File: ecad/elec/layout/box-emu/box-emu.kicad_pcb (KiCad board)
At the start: 2 copper layers, 72.5 x 63.9 mm, 68 parts

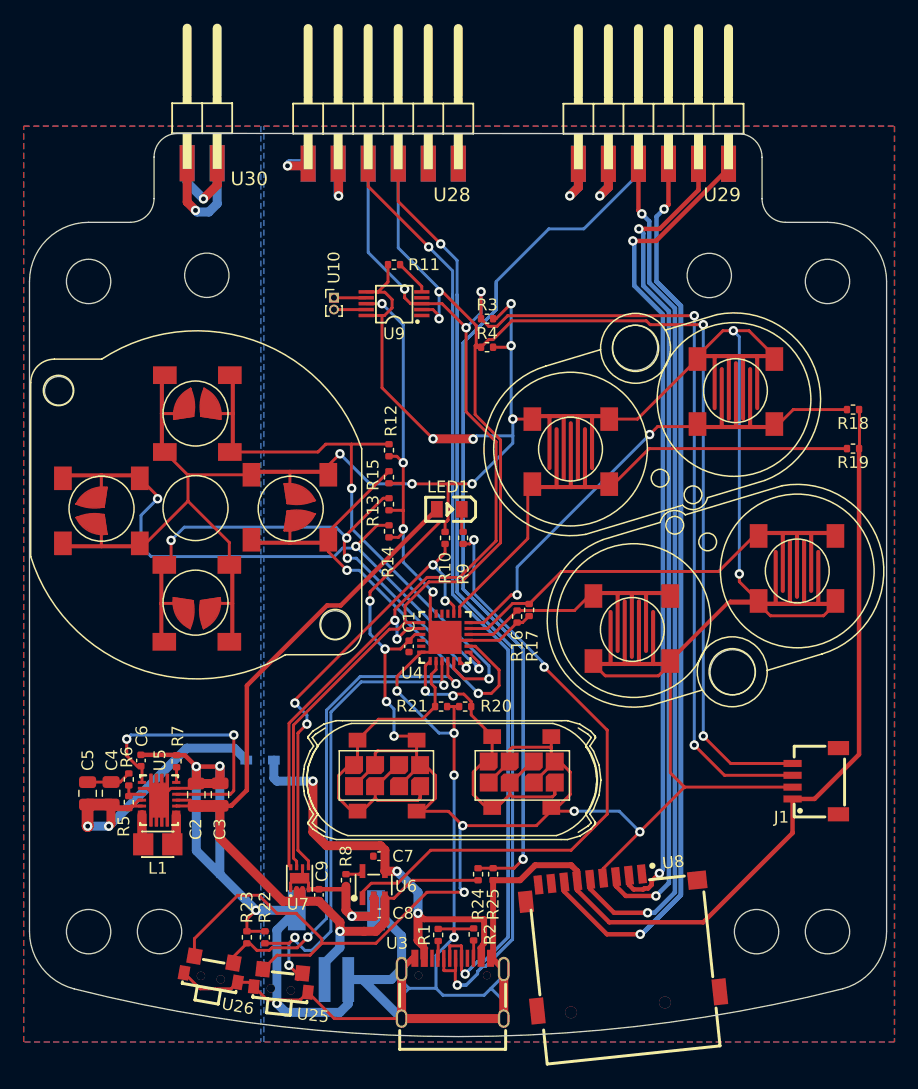
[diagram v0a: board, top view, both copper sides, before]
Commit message: Fix/atopile ecad (#82)
* fix(ecad): Fix bugs in atopile version of the design
* Add missing pullup resistors to AW9523 RSTN and INTN lines
* Fix I/O configuration for AW9523 so that all the inputs go to the same port pins as the previous version of the electronics

* minor cleanup to box3 after update to at 0.2.58

* fix udpate max17038 pullup to properly go to alert line after other fix

* typo

* update layout

* minor update to layout

* fix(buttons): pulldown -> pullup (so they are active low)

* update buttons to be pullup instead of pulldown; change led to be powered off VBUS instead of vbat

* update button footprints - start/select better aligned and all buttons have extra wires to ensure connections

* add net names and ensure packages are specified

* update box-emu-base layout

* update box-emu and box-3-emu layouts

* udpate to kicad 8

* add net name overrides and update all boards

* update atopile action to kicad 8

* comment out blender render
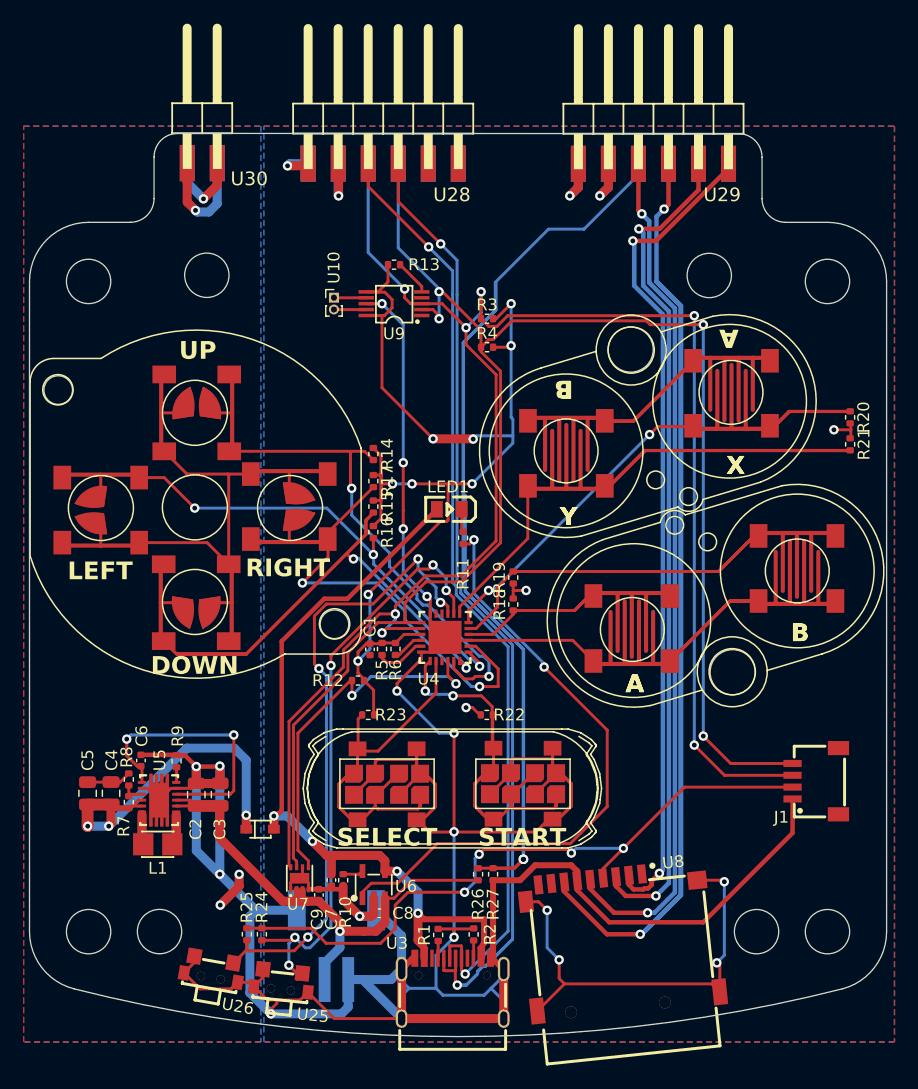
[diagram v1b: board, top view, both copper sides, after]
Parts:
- removed the R12 at (140.4, 96.7)
- removed the R13 at (140.4, 101.3)
- added R24: 62.5mW Thick Film Resistors 50V ±100ppm/℃ ±1% 10kΩ 0402 Chi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, lib:R0402, F.Cu at (129.7, 137.6)
- added R25: 62.5mW Thick Film Resistors 50V ±100ppm/℃ ±1% 10kΩ 0402 Chi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, lib:R0402, F.Cu at (128.4, 137.6)
- added R5: 62.5mW Thick Film Resistors 50V ±100ppm/℃ ±1% 10kΩ 0402 Chi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, lib:R0402, F.Cu at (139.8, 113.5)
- added R6: 62.5mW Thick Film Resistors 50V ±100ppm/℃ ±1% 10kΩ 0402 Chi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, lib:R0402, F.Cu at (141.0, 113.5)
- DS1: moved to F.Cu
- R7: renamed from R5; value 62.5mW Thick Film Resistors 50V ±100ppm/℃ ±1% 243kΩ 0402 Chip Resistor - Surface Mount ROHS -> 62.5mW Thick Film Resistors ±100ppm/℃ ±1% 243kΩ 0402 Chip Resistor - Surface Mount ROHS
- moved R21 41.1 mm to (179.4, 96.2), turned to -90 degrees
- moved R20 40.7 mm to (179.4, 93.9), turned to 90 degrees
- moved R18 33.1 mm to (150.9, 109.7), turned to -90 degrees
- moved R19 30.7 mm to (150.9, 107.5), turned to 90 degrees
- moved R22 26.6 mm to (148.7, 119.1), turned to 0 degrees
- moved R23 21.4 mm to (138.6, 119.1), turned to 180 degrees
- moved R17 17.1 mm to (139.1, 99.3), turned to -90 degrees
- moved R12 14.1 mm to (137.8, 116.2), turned to 0 degrees
- moved R16 14.1 mm to (139.1, 103.6), turned to -90 degrees
- moved R14 6.67 mm to (139.1, 97.0), turned to -90 degrees
- moved DS1 5.84 mm to (129.5, 128.8)
- moved C7 4.50 mm to (135.5, 133.1), turned to -90 degrees
- moved C1 3.31 mm to (138.8, 113.5)
- moved R15 2.81 mm to (139.1, 101.5), turned to -90 degrees
- moved U23 0.99 mm to (151.7, 124.9)
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- renumbered R8 to R10, R9 to R11, R10 to R12, R11 to R13, R24 to R26, R25 to R27, R6 to R8, R7 to R9
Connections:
- net a renamed box.drv2605.chip-a
- net b renamed box.drv2605.chip-b
- net box-vcc-1 renamed vcc_5v
- C1 pad 1: box-vcc -> vcc_3v3
- C2 pad 1: box-vcc-2 -> vbat
- C3 pad 1: box-vcc-2 -> vbat
- C7 pad 1: box-vcc-3 -> vbus
- C8 pad 1: box-vcc-2 -> vbat
- C9 pad 1: box-vcc-2 -> vbat
- DS1 pad 2: box-vcc-3 -> vbus
- J1 pad 2: box-vcc -> vcc_3v3
- LED1 pad 1: box-vcc-2 -> vbus
- R12 pad 1: p1_4 -> p1_3
- R12 pad 2: box-vcc -> vcc_3v3
- R13 pad 2: box-vcc -> vcc_3v3
- R14 pad 1: box-gnd -> vcc_3v3
- R14 pad 2: p0_2 -> up
- R15 pad 1: box-gnd -> vcc_3v3
- R15 pad 2: p0_3 -> down
- R16 pad 1: box-gnd -> vcc_3v3
- R16 pad 2: p0_4 -> left
- R17 pad 1: box-gnd -> vcc_3v3
- R17 pad 2: p0_5 -> right
- R18 pad 1: box-gnd -> vcc_3v3
- R18 pad 2: p0_6 -> box.io-a
- R19 pad 1: box-gnd -> vcc_3v3
- R19 pad 2: p0_7 -> box.io-b
- R20 pad 1: box-gnd -> vcc_3v3
- R20 pad 2: p1_0 -> x
- R21 pad 1: box-gnd -> vcc_3v3
- R21 pad 2: p1_1 -> y
- R22 pad 1: box-gnd -> vcc_3v3
- R22 pad 2: p1_2 -> start
- R23 pad 1: box-gnd -> vcc_3v3
- R23 pad 2: p1_3 -> select
- R26 pad 1: box-vcc-2 -> vbat
- R3 pad 2: box-vcc -> vcc_3v3
- R4 pad 2: box-vcc -> vcc_3v3
- U12 pad 1: p0_0 -> up
- U12 pad 2: box-vcc -> box-gnd
- U12 pad 3: p0_0 -> up
- U12 pad 4: box-vcc -> box-gnd
- U13 pad 1: p0_1 -> down
- U13 pad 2: box-vcc -> box-gnd
- U13 pad 3: p0_1 -> down
- U13 pad 4: box-vcc -> box-gnd
- U14 pad 1: p0_2 -> left
- U14 pad 2: box-vcc -> box-gnd
- U14 pad 3: p0_2 -> left
- U14 pad 4: box-vcc -> box-gnd
- U15 pad 1: p0_3 -> right
- U15 pad 2: box-vcc -> box-gnd
- U15 pad 3: p0_3 -> right
- U15 pad 4: box-vcc -> box-gnd
- U17 pad 1: p0_4 -> box.io-a
- U17 pad 2: box-vcc -> box-gnd
- U17 pad 3: p0_4 -> box.io-a
- U17 pad 4: box-vcc -> box-gnd
- U18 pad 1: p0_5 -> box.io-b
- U18 pad 2: box-vcc -> box-gnd
- U18 pad 3: p0_5 -> box.io-b
- U18 pad 4: box-vcc -> box-gnd
- U2 pad 1: box-vcc-2 -> vbat
- U20 pad 1: p0_6 -> x
- U20 pad 2: box-vcc -> box-gnd
- U20 pad 3: p0_6 -> x
- U20 pad 4: box-vcc -> box-gnd
- U21 pad 1: p0_7 -> y
- U21 pad 2: box-vcc -> box-gnd
- U21 pad 3: p0_7 -> y
- U21 pad 4: box-vcc -> box-gnd
- U23 pad 1: p1_0 -> start
- U23 pad 2: box-vcc -> box-gnd
- U23 pad 3: p1_0 -> start
- U23 pad 4: box-vcc -> box-gnd
- U24 pad 1: p1_1 -> select
- U24 pad 2: box-vcc -> box-gnd
- U24 pad 3: p1_1 -> select
- U24 pad 4: box-vcc -> box-gnd
- U25 pad 1: p1_2 -> vol_up
- U25 pad 2: box-vcc -> box-gnd
- U26 pad 1: p1_3 -> vol_down
- U26 pad 2: box-vcc -> box-gnd
- U28 pad 11: box-vcc -> vcc_3v3
- U28 pad 12: box-vcc -> vcc_3v3
- U29 pad 11: box-vcc -> vcc_3v3
- U29 pad 12: box-vcc -> vcc_3v3
- U3 pad A4: box-vcc-3 -> vbus
- U3 pad A9: box-vcc-3 -> vbus
- U3 pad B4: box-vcc-3 -> vbus
- U3 pad B9: box-vcc-3 -> vbus
- U4 pad 1: p1_0 -> start
- U4 pad 10: p0_4 -> box.io-a
- U4 pad 11: p0_5 -> box.io-b
- U4 pad 12: p0_6 -> x
- U4 pad 13: p0_7 -> y
- U4 pad 14: p1_4 -> vol_up
- U4 pad 15: p1_5 -> vol_down
- U4 pad 2: p1_1 -> select
- U4 pad 21: box-vcc -> vcc_3v3
- U4 pad 5: p0_0 -> up
- U4 pad 6: p0_1 -> down
- U4 pad 7: p0_2 -> left
- U4 pad 8: p0_3 -> right
- U5 pad 10: box-vcc-2 -> vbat
- U5 pad 11: box-vcc-2 -> vbat
- U6 pad 3: box-vcc-2 -> vbat
- U6 pad 4: box-vcc-3 -> vbus
- U7 pad 2: box-vcc-2 -> vbat
- U7 pad 3: box-vcc-2 -> vbat
- U7 pad 5: p1_4 -> p1_3
- U8 pad 4: box-vcc -> vcc_3v3
- U9 pad 10: box-vcc -> vcc_3v3
- U9 pad 6: box-vcc -> vcc_3v3
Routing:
- net box-vcc: track 301.1 -> 0.00 mm, vias 20 -> 0
- net vcc_3v3: track 0.00 -> 170.7 mm, vias 0 -> 18
- net box-gnd: track 347.0 -> 462.7 mm
- net box.io-b: track 0.00 -> 77.7 mm
- net box-vcc-2: track 77.6 -> 0.00 mm, vias 1 -> 0
- net down: track 0.00 -> 69.4 mm, vias 0 -> 2
- net vbus: track 0.00 -> 68.5 mm, vias 0 -> 4
- net y: track 0.00 -> 63.1 mm
- net dp: track 141.0 -> 79.5 mm
- net dm: track 143.2 -> 86.8 mm
- net vol_down: track 0.00 -> 52.9 mm, vias 0 -> 4
- net vol_up: track 0.00 -> 51.1 mm, vias 0 -> 5
- net up: track 0.00 -> 47.6 mm, vias 0 -> 2
- net x: track 0.00 -> 47.0 mm, vias 0 -> 2
- net p0_2: track 45.9 -> 0.00 mm, vias 3 -> 0
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- added copper zone on B.Cu, net vcc_3v3
- removed copper zone on B.Cu, net box-vcc
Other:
- board text added: "A"
- board text added: "B"
- board text added: "DOWN"
- board text added: "LEFT"
- board text added: "RIGHT"
- board text added: "SELECT"
- board text added: "START"
- board text added: "UP"
- board text added: "X"
- board text added: "Y"
